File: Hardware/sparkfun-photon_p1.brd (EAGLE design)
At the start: 68.6 x 53.3 mm, 53 parts, among them U1 WM-N-BM-14

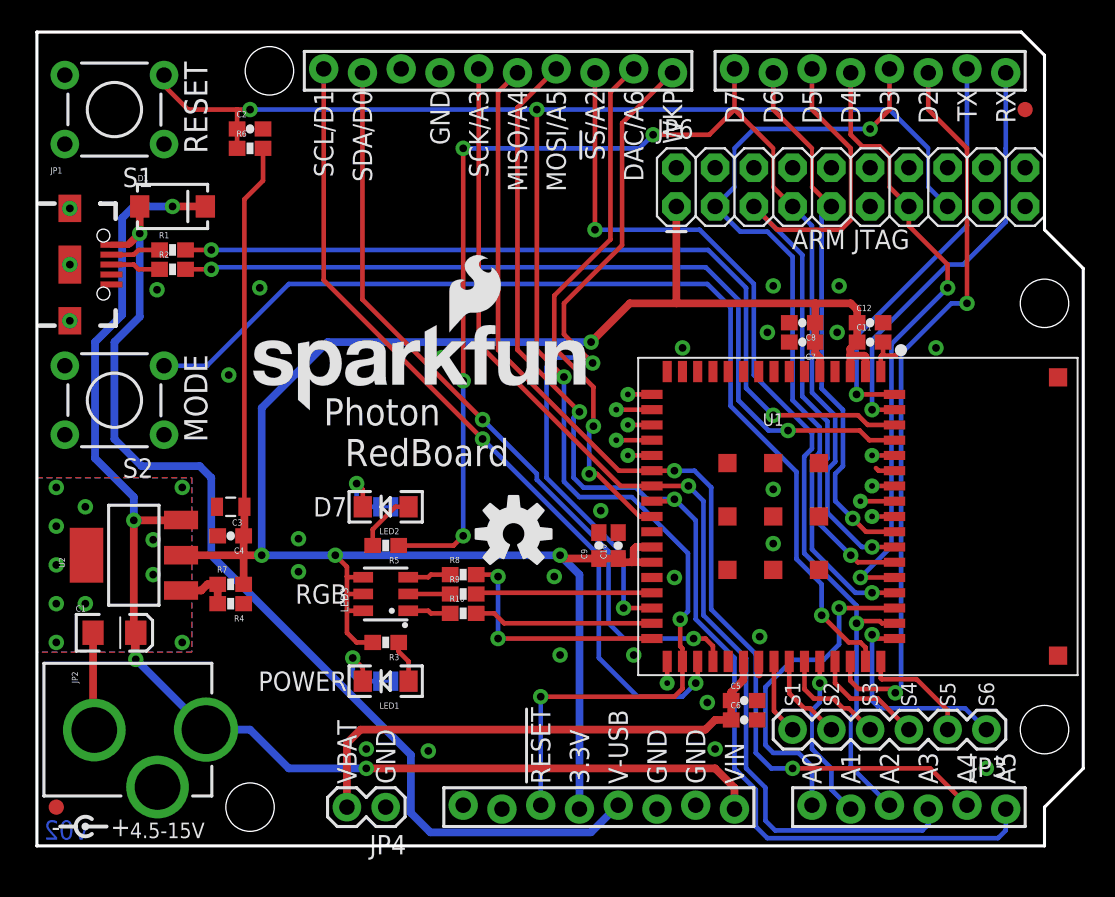
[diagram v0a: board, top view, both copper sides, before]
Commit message: Swapping WKP and DAC pins (maps PWM better).
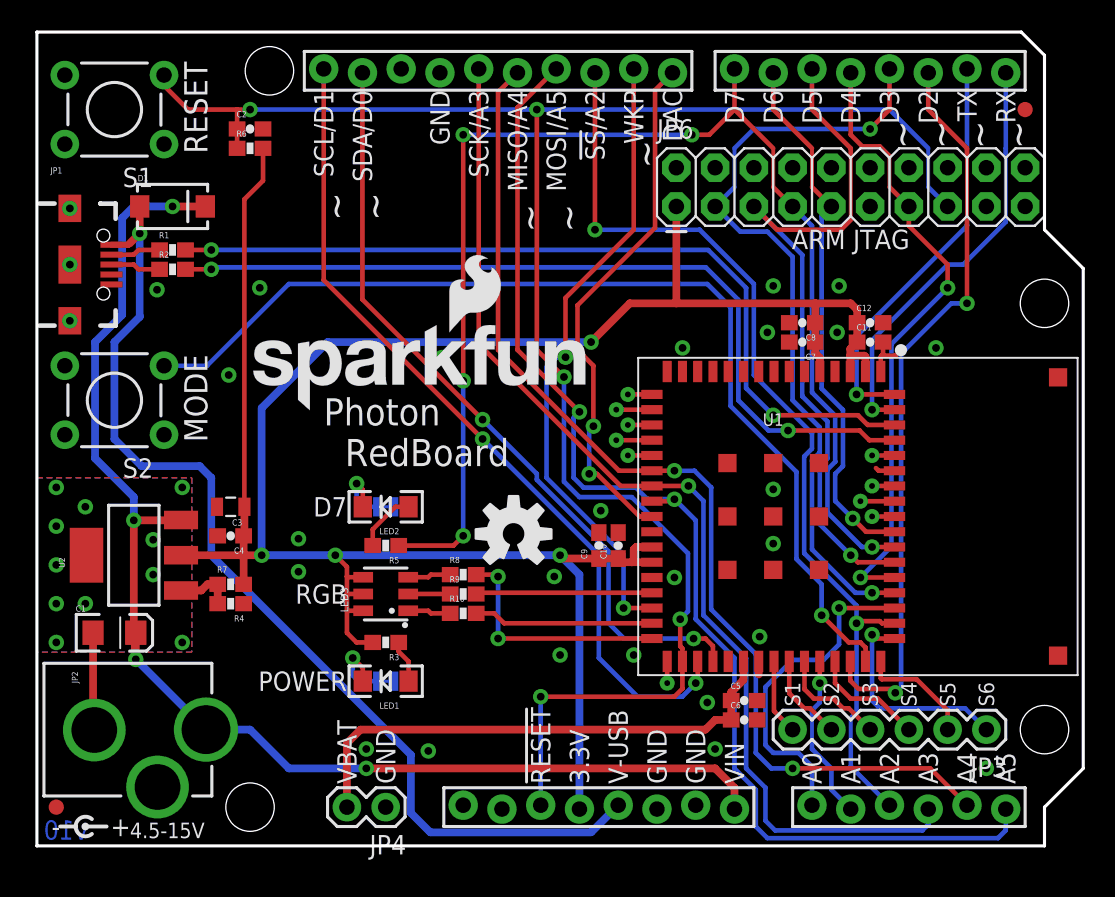
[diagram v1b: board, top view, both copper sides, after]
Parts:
- added LOGO3: SFE_LOGO_NAME_FLAME.4_INCH, SparkFun-Aesthetics:SFE_LOGO_NAME_FLAME_.4
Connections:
- net DAC: now also JP5.D8; no longer JP5.D9
- net WKP: now also JP5.D9; no longer JP5.D8
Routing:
- net WKP: track 45.9 -> 42.0 mm
- net D7(JTAG_TMS): track 86.1 -> 86.6 mm
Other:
- board text added: "DAC"
- board text added: "v10"
- board text added: "~"
- board text removed: "DAC/A6"
- board text removed: "v02"
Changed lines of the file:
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@@
 <text x="48.26" y="49.53" size="1.27" layer="21" font="vector" ratio="15" rot="R90" align="center-right">D6</text>
 <text x="45.72" y="49.53" size="1.27" layer="21" font="vector" ratio="15" rot="R90" align="center-right">D7</text>
-<text x="39.116" y="49.53" size="1.27" layer="21" font="vector" ratio="15" rot="R90" align="center-right">DAC/A6</text>
+<text x="41.656" y="49.53" size="1.27" layer="21" font="vector" ratio="15" rot="R90" align="center-right">DAC</text>
 <text x="36.576" y="49.53" size="1.27" layer="21" font="vector" ratio="15" rot="R90" align="center-right">!SS!/A2</text>
 <text x="34.036" y="49.53" size="1.27" layer="21" font="vector" ratio="15" rot="R90" align="center-right">MOSI/A5</text>
@@
 <text x="28.956" y="49.53" size="1.27" layer="21" font="vector" ratio="15" rot="R90" align="center-right">SCK/A3</text>
 <text x="26.416" y="49.53" size="1.27" layer="21" font="vector" ratio="15" rot="R90" align="center-right">GND</text>
-<text x="41.656" y="49.53" size="1.27" layer="21" font="vector" ratio="15" rot="R90" align="center-right">WKP</text>
+<text x="39.116" y="49.53" size="1.27" layer="21" font="vector" ratio="15" rot="R90" align="center-right">WKP</text>
 <text x="21.336" y="49.53" size="1.27" layer="21" font="vector" ratio="15" rot="R90" align="center-right">SDA/D0</text>
 <text x="18.796" y="49.53" size="1.27" layer="21" font="vector" ratio="15" rot="R90" align="center-right">SCL/D1</text>
@@
 <text x="20.32" y="4.064" size="1.27" layer="21" font="vector" ratio="15" rot="R90" align="center-left">VBAT</text>
 <text x="22.86" y="4.064" size="1.27" layer="21" font="vector" ratio="15" rot="R90" align="center-left">GND</text>
-<text x="1.905" y="1.6764" size="1.27" layer="16" font="vector" ratio="15" rot="MR0" align="top-center">v02</text>
+<text x="1.905" y="1.6764" size="1.27" layer="16" font="vector" ratio="15" rot="MR0" align="top-center">v10</text>
 <text x="6.096" y="1.016" size="1.016" layer="21" font="vector" ratio="15" align="center-left">4.5-15V</text>
 <wire x1="1.524" y1="1.27" x2="2.54" y2="1.27" width="0.254" layer="21"/>
@@
 <text x="55.245" y="21.59" size="0.8128" layer="22" font="vector" ratio="15" rot="MR0" align="center-right">BTCX-RF_ACT</text>
 <text x="54.483" y="22.59" size="0.8128" layer="22" font="vector" ratio="15" rot="MR0" align="center-right">BTCX-STAT</text>
-<text x="24.003" y="10.795" size="0.8128" layer="22" font="vector" ratio="15" rot="MR0" align="center-right">PWR
+<text x="21.59" y="10.795" size="0.8128" layer="22" font="vector" ratio="15" rot="MR180" align="center-right">PWR
 LED</text>
-<text x="24.003" y="22.225" size="0.8128" layer="22" font="vector" ratio="15" rot="MR0" align="center-right">D7
+<text x="21.59" y="22.225" size="0.8128" layer="22" font="vector" ratio="15" rot="MR180" align="center-right">D7
 LED</text>
+<text x="59.182" y="46.609" size="1.778" layer="21" font="vector" ratio="15" rot="R90" align="center">~</text>
+<text x="56.642" y="46.609" size="1.778" layer="21" font="vector" ratio="15" rot="R90" align="center">~</text>
+<text x="61.722" y="46.609" size="1.778" layer="21" font="vector" ratio="15" rot="R90" align="center">~</text>
+<text x="64.262" y="46.609" size="1.778" layer="21" font="vector" ratio="15" rot="R90" align="center">~</text>
+<text x="39.878" y="45.339" size="1.778" layer="21" font="vector" ratio="15" rot="R90" align="center">~</text>
+<text x="34.798" y="41.148" size="1.778" layer="21" font="vector" ratio="15" rot="R90" align="center">~</text>
+<text x="32.258" y="41.148" size="1.778" layer="21" font="vector" ratio="15" rot="R90" align="center">~</text>
+<text x="22.098" y="41.91" size="1.778" layer="21" font="vector" ratio="15" rot="R90" align="center">~</text>
+<text x="19.558" y="41.91" size="1.778" layer="21" font="vector" ratio="15" rot="R90" align="center">~</text>
 </plain>
 <attributes>
@@
 <element name="SJ1" library="SparkFun-Passives" package="PAD-JUMPER-2-NC_BY_TRACE_YES_SILK" value="PWR-LED" x="22.86" y="10.795" rot="MR0"/>
 <element name="SJ2" library="SparkFun-Passives" package="PAD-JUMPER-2-NC_BY_TRACE_YES_SILK" value="D7-LED" x="22.86" y="22.225" rot="MR0"/>
+<element name="LOGO3" library="SparkFun-Aesthetics" package="SFE_LOGO_NAME_FLAME_.4" value="SFE_LOGO_NAME_FLAME.4_INCH" x="40.64" y="6.35" rot="MR45"/>
 </elements>
 <signals>
@@
 <wire x1="27.94" y1="20.32" x2="27.94" y2="30.48" width="0.3048" layer="16"/>
 <via x="27.94" y="30.48" extent="1-16" drill="0.508"/>
-<wire x1="27.94" y1="30.48" x2="27.94" y2="45.72" width="0.3048" layer="1"/>
-<via x="27.94" y="45.72" extent="1-16" drill="0.508"/>
-<wire x1="27.94" y1="45.72" x2="39.497" y2="45.72" width="0.3048" layer="16"/>
-<wire x1="39.497" y1="45.72" x2="40.386" y2="46.609" width="0.3048" layer="16"/>
-<via x="40.386" y="46.609" extent="1-16" drill="0.508"/>
-<wire x1="40.386" y1="46.609" x2="44.069" y2="46.609" width="0.3048" layer="1"/>
+<wire x1="27.94" y1="30.48" x2="27.94" y2="46.609" width="0.3048" layer="1"/>
+<via x="27.94" y="46.609" extent="1-16" drill="0.508"/>
+<wire x1="27.94" y1="46.609" x2="42.926" y2="46.609" width="0.3048" layer="16"/>
+<via x="42.926" y="46.609" extent="1-16" drill="0.508"/>
+<wire x1="42.926" y1="46.609" x2="44.069" y2="46.609" width="0.3048" layer="1"/>
 <wire x1="44.069" y1="46.609" x2="45.72" y2="48.26" width="0.3048" layer="1"/>
 <wire x1="50.8" y1="40.64" x2="49.53" y2="41.91" width="0.3048" layer="16"/>
@@
 </signal>
 <signal name="DAC">
-<contactref element="JP5" pad="D9"/>
 <contactref element="U1" pad="24"/>
 <via x="36.195" y="24.384" extent="1-16" drill="0.508"/>
 <via x="36.4744" y="27.5082" extent="1-16" drill="0.508"/>
-<wire x1="37.592" y1="49.403" x2="39.116" y2="50.927" width="0.3048" layer="1"/>
-<wire x1="37.592" y1="39.751" x2="37.592" y2="49.403" width="0.3048" layer="1"/>
-<wire x1="37.592" y1="39.751" x2="33.909" y2="36.068" width="0.3048" layer="1"/>
-<wire x1="33.909" y1="36.068" x2="33.909" y2="32.639" width="0.3048" layer="1"/>
-<wire x1="33.909" y1="32.639" x2="36.4744" y2="30.0736" width="0.3048" layer="1"/>
 <wire x1="39.497" y1="21.59" x2="40.31" y2="21.59" width="0.3048" layer="1"/>
 <wire x1="40.64" y1="21.59" x2="40.31" y2="21.59" width="0.3048" layer="1"/>
@@
 <wire x1="36.195" y1="24.384" x2="36.195" y2="27.2288" width="0.3048" layer="16"/>
 <wire x1="36.195" y1="27.2288" x2="36.4744" y2="27.5082" width="0.3048" layer="16"/>
-<wire x1="36.4744" y1="27.5082" x2="36.4744" y2="30.0736" width="0.3048" layer="1"/>
+<wire x1="36.4744" y1="27.5082" x2="36.4744" y2="31.4706" width="0.3048" layer="1"/>
+<contactref element="JP5" pad="D8"/>
+<wire x1="36.4744" y1="31.4706" x2="35.433" y2="32.512" width="0.3048" layer="1"/>
+<wire x1="35.433" y1="32.512" x2="35.433" y2="35.433" width="0.3048" layer="1"/>
+<wire x1="35.433" y1="35.433" x2="40.513" y2="40.513" width="0.3048" layer="1"/>
+<wire x1="40.513" y1="40.513" x2="40.513" y2="49.53" width="0.3048" layer="1"/>
+<wire x1="40.513" y1="49.53" x2="41.656" y2="50.673" width="0.3048" layer="1"/>
 </signal>
 <signal name="A5/SPI_MOSI">
@@
 <wire x1="38.45" y1="19.081" x2="33.401" y2="24.13" width="0.3048" layer="16"/>
 <wire x1="38.45" y1="15.59" x2="38.45" y2="19.081" width="0.3048" layer="16"/>
-<contactref element="JP5" pad="D8"/>
 <wire x1="33.401" y1="24.13" x2="33.401" y2="31.369" width="0.3048" layer="16"/>
-<via x="36.4236" y="31.6484" extent="1-16" drill="0.508"/>
-<wire x1="38.354" y1="47.371" x2="41.656" y2="50.673" width="0.3048" layer="1"/>
-<wire x1="38.354" y1="39.37" x2="38.354" y2="47.371" width="0.3048" layer="1"/>
-<wire x1="34.544" y1="35.56" x2="38.354" y2="39.37" width="0.3048" layer="1"/>
-<wire x1="34.036" y1="32.004" x2="33.401" y2="31.369" width="0.3048" layer="16"/>
-<wire x1="36.4236" y1="31.6484" x2="34.544" y2="33.528" width="0.3048" layer="1"/>
-<wire x1="34.544" y1="33.528" x2="34.544" y2="35.56" width="0.3048" layer="1"/>
-<wire x1="34.036" y1="32.004" x2="36.068" y2="32.004" width="0.3048" layer="16"/>
-<wire x1="36.068" y1="32.004" x2="36.4236" y2="31.6484" width="0.3048" layer="16"/>
+<via x="34.6456" y="32.0294" extent="1-16" drill="0.508"/>
+<wire x1="34.0614" y1="32.0294" x2="33.401" y2="31.369" width="0.3048" layer="16"/>
 <contactref element="U1" pad="30"/>
 <wire x1="40.31" y1="15.59" x2="38.45" y2="15.59" width="0.3048" layer="1"/>
+<contactref element="JP5" pad="D9"/>
+<wire x1="34.6456" y1="32.0294" x2="34.0614" y2="32.0294" width="0.3048" layer="16"/>
+<wire x1="34.6456" y1="32.0294" x2="34.6456" y2="35.9156" width="0.3048" layer="1"/>
+<wire x1="34.6456" y1="35.9156" x2="39.116" y2="40.386" width="0.3048" layer="1"/>
+<wire x1="39.116" y1="40.386" x2="39.116" y2="50.927" width="0.3048" layer="1"/>
 </signal>
 <signal name="VBAT">

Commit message: Moving vias to avoid silk.
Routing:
- net GND: vias 28 -> 29
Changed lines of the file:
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@@
 <via x="25.654" y="6.223" extent="1-16" drill="0.508"/>
 <via x="21.59" y="6.35" extent="1-16" drill="0.508"/>
-<via x="26.543" y="32.004" extent="1-16" drill="0.508"/>
 <via x="12.573" y="30.861" extent="1-16" drill="0.508"/>
 <contactref element="SJ1" pad="1"/>
 <contactref element="SJ2" pad="1"/>
+<via x="16.002" y="28.194" extent="1-16" drill="0.508"/>
+<via x="26.67" y="33.274" extent="1-16" drill="0.508"/>
 </signal>
 <signal name="3.3V">
@@
 <wire x1="51.015" y1="33.02" x2="51.015" y2="32.297" width="0.508" layer="1"/>
 <wire x1="14.732" y1="19.05" x2="14.732" y2="28.702" width="0.508" layer="16"/>
-<wire x1="14.732" y1="28.702" x2="19.05" y2="33.02" width="0.508" layer="16"/>
-<wire x1="19.05" y1="33.02" x2="36.322" y2="33.02" width="0.508" layer="16"/>
-<via x="36.322" y="33.02" extent="1-16" drill="0.508"/>
+<wire x1="14.732" y1="28.702" x2="20.32" y2="34.29" width="0.508" layer="16"/>
+<wire x1="20.32" y1="34.29" x2="37.592" y2="34.29" width="0.508" layer="16"/>
+<via x="37.592" y="34.29" extent="1-16" drill="0.508"/>
 <via x="34.29" y="19.05" extent="1-16" drill="0.508"/>
 <wire x1="34.29" y1="19.05" x2="35.56" y2="17.78" width="0.508" layer="16"/>
@@
 <via x="19.558" y="19.05" extent="1-16" drill="0.508"/>
 <wire x1="34.29" y1="19.05" x2="19.558" y2="19.05" width="0.508" layer="16"/>
-<wire x1="36.322" y1="33.02" x2="38.862" y2="35.56" width="0.508" layer="1"/>
+<wire x1="37.592" y1="34.29" x2="38.862" y2="35.56" width="0.508" layer="1"/>
 <wire x1="38.862" y1="35.56" x2="41.91" y2="35.56" width="0.508" layer="1"/>
 <wire x1="41.91" y1="35.56" x2="51.015" y2="35.56" width="0.508" layer="1"/>
@@
 <wire x1="27.305" y1="19.685" x2="27.94" y2="20.32" width="0.3048" layer="1"/>
 <via x="27.94" y="20.32" extent="1-16" drill="0.508"/>
-<wire x1="27.94" y1="20.32" x2="27.94" y2="30.48" width="0.3048" layer="16"/>
-<via x="27.94" y="30.48" extent="1-16" drill="0.508"/>
-<wire x1="27.94" y1="30.48" x2="27.94" y2="46.609" width="0.3048" layer="1"/>
+<wire x1="27.94" y1="20.32" x2="27.94" y2="31.623" width="0.3048" layer="16"/>
+<via x="27.94" y="31.623" extent="1-16" drill="0.508"/>
+<wire x1="27.94" y1="31.623" x2="27.94" y2="46.609" width="0.3048" layer="1"/>
 <via x="27.94" y="46.609" extent="1-16" drill="0.508"/>
 <wire x1="27.94" y1="46.609" x2="42.926" y2="46.609" width="0.3048" layer="16"/>
@@
 <contactref element="U1" pad="35"/>
 <via x="43.183" y="10.668" extent="1-16" drill="0.508"/>
-<wire x1="18.796" y1="50.927" x2="18.796" y2="37.084" width="0.3048" layer="1"/>
+<wire x1="18.796" y1="50.927" x2="18.796" y2="36.576" width="0.3048" layer="1"/>
 <wire x1="39.37" y1="9.779" x2="36.83" y2="12.319" width="0.3048" layer="16"/>
-<wire x1="36.83" y1="12.319" x2="36.83" y2="19.05" width="0.3048" layer="16"/>
-<via x="29.21" y="26.67" extent="1-16" drill="0.508"/>
-<wire x1="29.21" y1="26.67" x2="18.796" y2="37.084" width="0.3048" layer="1"/>
-<wire x1="36.83" y1="19.05" x2="29.21" y2="26.67" width="0.3048" layer="16"/>
+<wire x1="36.83" y1="12.319" x2="36.83" y2="18.542" width="0.3048" layer="16"/>
+<via x="31.75" y="23.622" extent="1-16" drill="0.508"/>
+<wire x1="31.75" y1="23.622" x2="18.796" y2="36.576" width="0.3048" layer="1"/>
+<wire x1="36.83" y1="18.542" x2="31.75" y2="23.622" width="0.3048" layer="16"/>
 <wire x1="43.31" y1="12.09" x2="43.31" y2="10.795" width="0.3048" layer="1"/>
 <wire x1="43.31" y1="10.795" x2="43.183" y2="10.668" width="0.3048" layer="1"/>
@@
 <contactref element="U1" pad="36"/>
 <via x="43.04" y="13.589" extent="1-16" drill="0.508"/>
-<wire x1="21.336" y1="50.673" x2="21.336" y2="35.814" width="0.3048" layer="1"/>
-<wire x1="21.336" y1="35.814" x2="29.21" y2="27.94" width="0.3048" layer="1"/>
-<via x="29.21" y="27.94" extent="1-16" drill="0.508"/>
-<wire x1="37.465" y1="19.304" x2="32.766" y2="24.003" width="0.3048" layer="16"/>
+<wire x1="21.336" y1="50.673" x2="21.336" y2="35.433" width="0.3048" layer="1"/>
+<wire x1="21.336" y1="35.433" x2="30.226" y2="26.543" width="0.3048" layer="1"/>
+<via x="30.226" y="26.543" extent="1-16" drill="0.508"/>
+<wire x1="37.465" y1="19.304" x2="30.226" y2="26.543" width="0.3048" layer="16"/>
 <wire x1="37.465" y1="14.605" x2="37.465" y2="19.304" width="0.3048" layer="16"/>
-<wire x1="32.766" y1="24.003" x2="32.766" y2="24.384" width="0.3048" layer="16"/>
-<wire x1="32.766" y1="24.384" x2="29.21" y2="27.94" width="0.3048" layer="16"/>
 <wire x1="44.31" y1="12.09" x2="44.31" y2="13.094" width="0.3048" layer="1"/>
 <wire x1="44.31" y1="13.094" x2="43.815" y2="13.589" width="0.3048" layer="1"/>

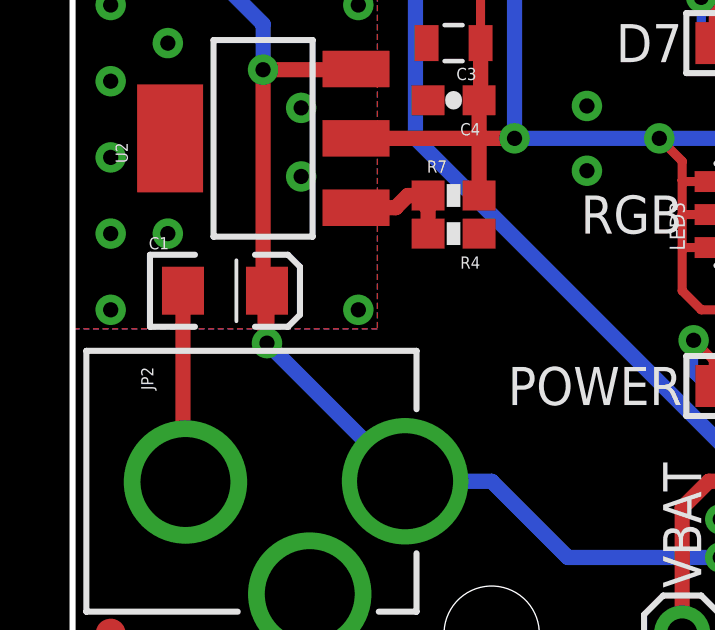
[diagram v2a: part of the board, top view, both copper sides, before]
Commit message: Cleaning up VIN trace.
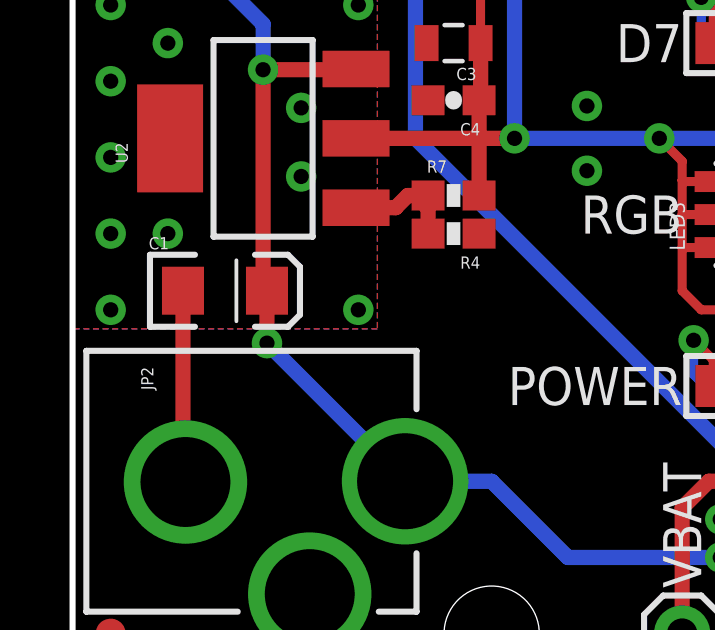
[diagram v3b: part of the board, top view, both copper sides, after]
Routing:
- net VIN: track 85.6 -> 83.8 mm
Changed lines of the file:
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@@
 <layer number="47" name="Measures" color="7" fill="1" visible="no" active="yes"/>
 <layer number="48" name="Document" color="7" fill="1" visible="no" active="yes"/>
-<layer number="49" name="Reference" color="7" fill="1" visible="yes" active="yes"/>
+<layer number="49" name="Reference" color="7" fill="1" visible="no" active="yes"/>
 <layer number="50" name="dxf" color="7" fill="1" visible="no" active="no"/>
 <layer number="51" name="tDocu" color="6" fill="1" visible="yes" active="yes"/>
@@
 <contactref element="JP2" pad="PWR"/>
 <contactref element="JP5" pad="VIN"/>
-<wire x1="6.48" y1="12.2238" x2="6.48" y2="13.97" width="0.508" layer="1"/>
-<wire x1="6.48" y1="13.97" x2="6.415" y2="14.035" width="0.508" layer="1"/>
-<wire x1="6.415" y1="14.035" x2="6.35" y2="14.1" width="0.508" layer="1"/>
+<wire x1="6.48" y1="13.97" x2="6.35" y2="14.1" width="0.508" layer="1"/>
 <wire x1="6.35" y1="14.1" x2="6.35" y2="21.3385" width="0.508" layer="1"/>
 <wire x1="11.04" y1="41.91" x2="8.89" y2="41.91" width="0.508" layer="1"/>
@@
 <wire x1="11.0838" y1="7.62" x2="6.48" y2="12.2238" width="0.508" layer="16"/>
 <via x="6.48" y="12.2238" extent="1-16" drill="0.508"/>
-<wire x1="6.48" y1="12.2238" x2="6.415" y2="12.2888" width="0.508" layer="1"/>
-<wire x1="6.415" y1="12.2888" x2="6.415" y2="14.035" width="0.508" layer="1"/>
+<wire x1="6.48" y1="13.97" x2="6.48" y2="12.2238" width="0.508" layer="1"/>
 </signal>
 <signal name="N$15">
